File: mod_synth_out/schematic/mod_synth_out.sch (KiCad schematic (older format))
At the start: 3 parts

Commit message: Initial clone of befaco (without cue)
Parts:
- removed J?: Headphones, symbol Connector:AudioJack3
- added C? (x4): 10uf, Capacitor_THT:CP_Radial_D5.0mm_P2.00mm, symbol Device:CP_Small
- added C? (x4): 10pf, Capacitor_THT:C_Disc_D9.0mm_W2.5mm_P5.00mm, symbol Device:C_Small
- added C? (x8): 100nf, Capacitor_THT:C_Disc_D9.0mm_W2.5mm_P5.00mm, symbol Device:C_Small
- added D? (x2): LED, symbol Device:LED
- added D? (x4): 1N4148, Diode_THT:D_DO-35_SOD27_P7.62mm_Horizontal, symbol Diode:1N4148
- added J?: L OUT, symbol Connector:AudioJack3_SwitchTR
- added J?: R OUT, symbol Connector:AudioJack3_SwitchTR
- added J?: Phones, symbol Connector:AudioJack3_SwitchTR
- added J?: Conn_02x08_Odd_Even, symbol Connector_Generic:Conn_02x08_Odd_Even
- added Q? (x2): 2N3904, Package_TO_SOT_THT:TO-92_Inline, symbol Transistor_BJT:2N3904
- added R? (x4): 100k, Resistor_THT:R_Axial_DIN0207_L6.3mm_D2.5mm_P10.16mm_Horizontal, symbol Device:R
- added R? (x2): 39k, Resistor_THT:R_Axial_DIN0207_L6.3mm_D2.5mm_P10.16mm_Horizontal, symbol Device:R
- added R? (x6): 1k, Resistor_THT:R_Axial_DIN0207_L6.3mm_D2.5mm_P10.16mm_Horizontal, symbol Device:R
- added R? (x8): 10k, Resistor_THT:R_Axial_DIN0207_L6.3mm_D2.5mm_P10.16mm_Horizontal, symbol Device:R
- added R? (x4): 75, Resistor_THT:R_Axial_DIN0207_L6.3mm_D2.5mm_P10.16mm_Horizontal, symbol Device:R
- added RV? (x4): 100k, symbol Device:R_POT_Dual_Separate
- added U? (x6): TL072, symbol Amplifier_Operational:TL072
- added U? (x6): NE5532, symbol Amplifier_Operational:NE5532
- J?: value R IN -> L IN; footprint (none) -> Connector_Audio:Jack_3.5mm_QingPu_WQP-PJ398SM_Vertical_CircularHoles
- J?: value L IN -> R IN; footprint (none) -> Connector_Audio:Jack_3.5mm_QingPu_WQP-PJ398SM_Vertical_CircularHoles
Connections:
- net GND: now reaches J?.S
- net GND: now also J?.S, C?.2, C?.2, J?.S, Q?.1 (E), Q?.1 (E), R?.2, R?.2, R?.2, R?.2, RV?.1, RV?.1, RV?.4, RV?.4, U?.3 (+), U?.3 (+), U?.5 (+), U?.5 (+), U?.5 (+), U?.5 (+)
- net IN_L: now reaches J?.T
- net IN_L: now also J?.TN, R?.2, R?.2
- net IN_R: now reaches J?.T
- net IN_R: now also R?.2, R?.2
- new net: J?.R, R?.1 (x2)
- new net: J?.T, R?.1 (x2)
- new net: J?.R, R?.1, R?.1
- new net: J?.T, R?.1, R?.1
- new net: C?.1, C?.1, R?.1, U?.1
- new net: C?.2, R?.1, R?.2, U?.2 (-)
- new net: C?.2, R?.1, R?.2, U?.6 (-)
- new net: C?.1, C?.1, R?.1, U?.7
- new net: C?.1, D?.1 (K), D?.2 (A), R?.1, R?.2, U?.1
- new net: R?.1, U?.2 (-)
- new net: R?.1, U?.6 (-)
- new net: C?.1, D?.1 (K), D?.2 (A), R?.1, R?.2, U?.7
- new net: R?.2, U?.1, U?.2 (-) (x2)
- new net: R?.1, R?.2, U?.3 (+), U?.7 (x2)
- new net: R?.1, R?.2, U?.6 (-) (x2)
- new net: C?.2, RV?.3, RV?.3
- new net: C?.2, RV?.6, RV?.6
- new net: D?.1 (K), R?.2 (x2)
- new net: Q?.3 (C), R?.1 (x2)
- new net: Q?.2 (B), R?.1 (x2)
- new net +12V: D?.1 (K), D?.1 (K), D?.2 (A), D?.2 (A)
- new net -12V: D?.2 (A), D?.2 (A)
- new net A_POT_ML: RV?.2
- new net A_POT_MR: RV?.5
- new net A_POT_PH_L: RV?.2
- new net A_POT_PH_R: RV?.5
- new net B_POT_ML: R?.2
- new net B_POT_MR: R?.2
- new net B_POT_PH_L: R?.2
- new net B_POT_PH_R: R?.2
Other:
- moved on the sheet: J?

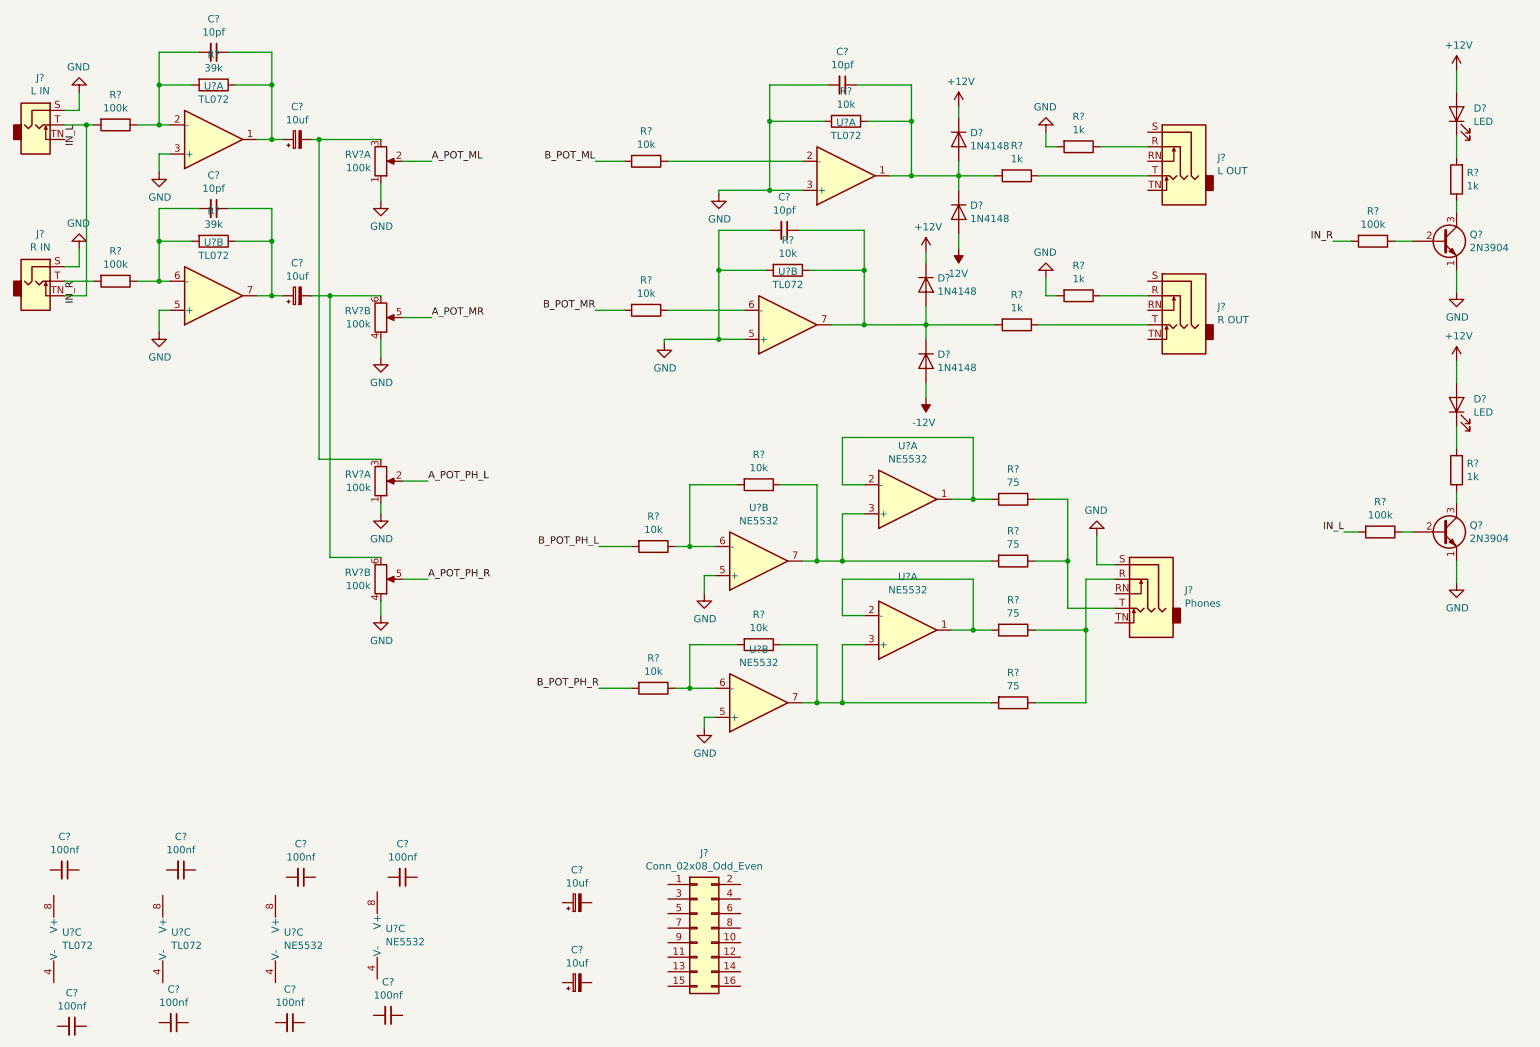
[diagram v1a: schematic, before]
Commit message: Attempt layout of output with through hole devices
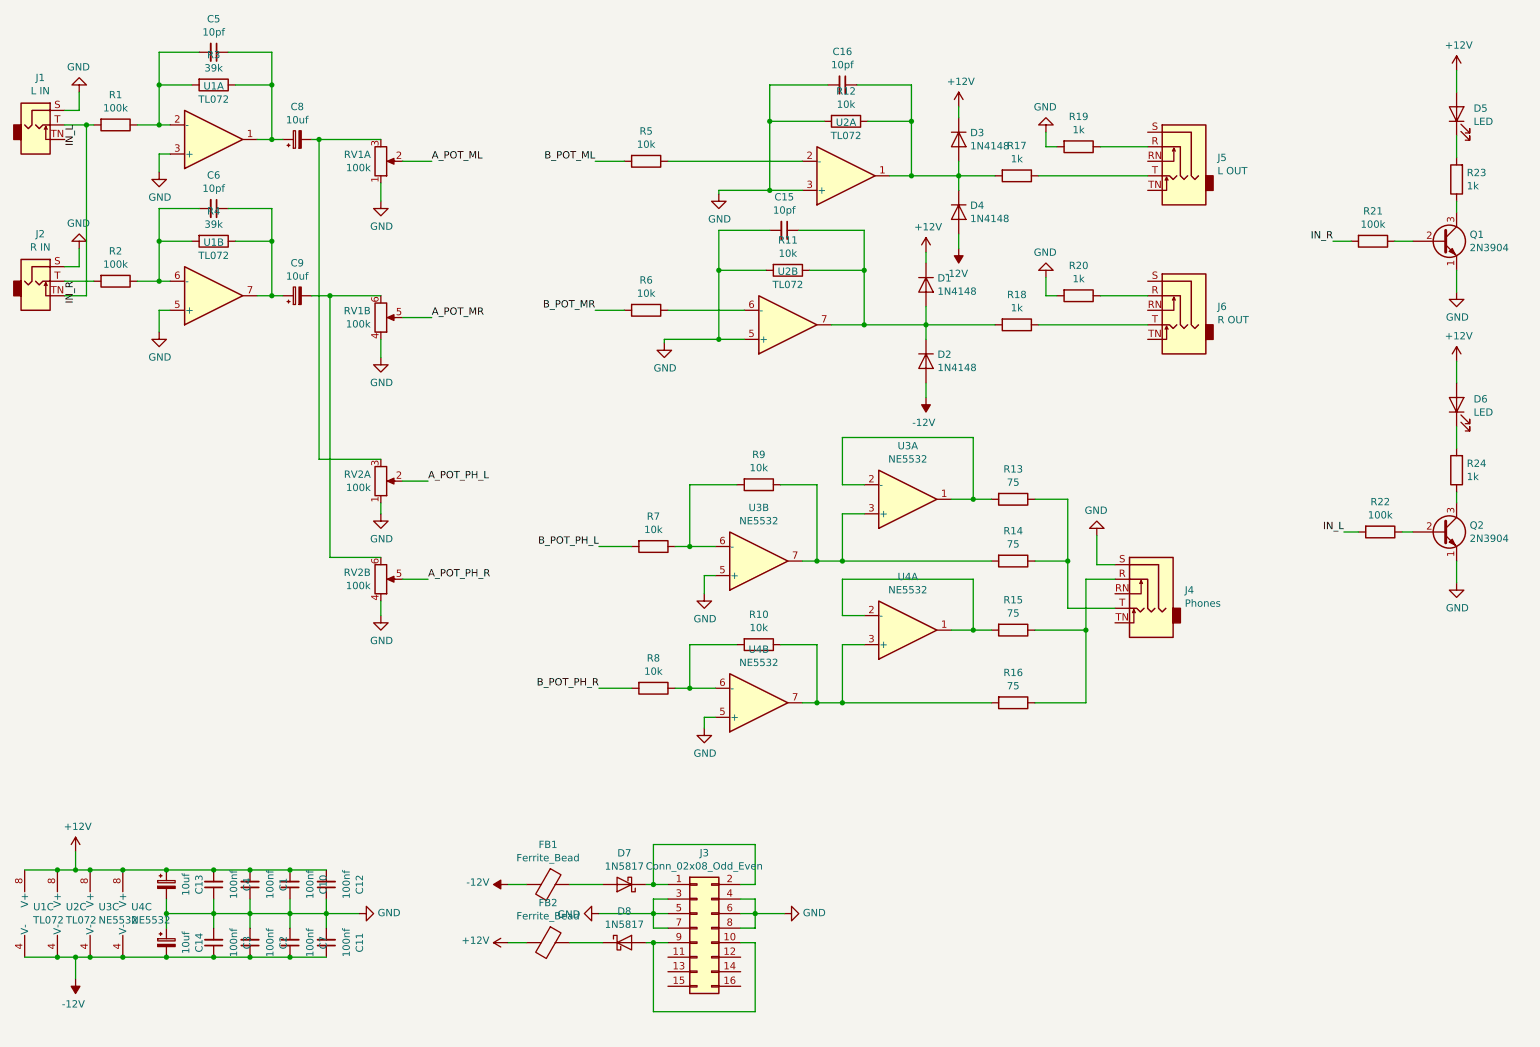
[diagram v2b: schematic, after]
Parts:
- added D7, D8: 1N5817, Diode_THT:D_DO-41_SOD81_P10.16mm_Horizontal, symbol Diode:1N5817
- added FB1, FB2: Ferrite_Bead, Resistor_THT:R_Axial_DIN0207_L6.3mm_D2.5mm_P10.16mm_Horizontal, symbol Device:Ferrite_Bead
- D5, D6: renamed from D?; footprint (none) -> LED_THT:LED_D5.0mm
- J3: renamed from J?; footprint (none) -> Connector_IDC:IDC-Header_2x08_P2.54mm_Vertical
- J4, J5, J6: renamed from J?; footprint (none) -> mod_synth:WQP-PJ612A-A
- RV1: renamed from RV?; footprint (none) -> Potentiometer_THT:Potentiometer_Alpha_RD902F-40-00D_Dual_Vertical_CircularHoles; Text (none) -> Volume
- RV1, RV2: renamed from RV?; footprint (none) -> Potentiometer_THT:Potentiometer_Alpha_RD902F-40-00D_Dual_Vertical_CircularHoles
- RV2: renamed from RV?; footprint (none) -> Potentiometer_THT:Potentiometer_Alpha_RD902F-40-00D_Dual_Vertical_CircularHoles; Text (none) -> Phones
- U1, U2, U3, U4: renamed from U?; footprint (none) -> Package_DIP:DIP-8_W7.62mm_Socket_LongPads
- gave numbers to parts that had none: 52
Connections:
- net +12V: now also C1.2, C10.2, C12.2, C13.1, C4.2, U1.8 (V+), U2.8 (V+), U3.8 (V+), U4.8 (V+), FB2.2
- net -12V: now also C11.1, C14.2, C2.1, C3.1, C7.1, U1.4 (V-), U2.4 (V-), U3.4 (V-), U4.4 (V-), FB1.2
- net GND: now also C1.1, C10.1, C11.2, C12.1, C13.2, C14.1, C2.2, C3.2, C4.1, C7.2, J3.3 (Pin_3), J3.4 (Pin_4), J3.5 (Pin_5), J3.6 (Pin_6), J3.7 (Pin_7), J3.8 (Pin_8)
- net at J3.1 (Pin_1): now also J3.2 (Pin_2), D7.1 (K)
- net at J3.10 (Pin_10): now also J3.9 (Pin_9), D8.2 (A)
- new net: D8.1 (K), FB2.1
- new net: D7.2 (A), FB1.1
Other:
- moved on the sheet: C1, C10, C11, C12, C13, C14, C2, C3, C4, C7, U1C, U2C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

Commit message: Attmept layout of output pcb on large pcb
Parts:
- added J7: Conn_01x07_Female, Connector_PinSocket_2.54mm:PinSocket_1x07_P2.54mm_Vertical, symbol Connector:Conn_01x07_Female
- added J8: Conn_01x07_Male, Connector_PinHeader_2.54mm:PinHeader_1x07_P2.54mm_Vertical, symbol Connector:Conn_01x07_Male
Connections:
- net +12V: now also J7.7 (Pin_7); no longer C10.2, D5.2 (A), D6.2 (A), U1.8 (V+)
- net -12V: now also J7.6 (Pin_6); no longer C7.1, U1.4 (V-)
- net A_POT_ML: now also J8.2 (Pin_2)
- net A_POT_MR: now also J8.3 (Pin_3)
- net A_POT_PH_L: now also J8.4 (Pin_4)
- net A_POT_PH_R: now also J8.5 (Pin_5)
- net B_POT_ML: now also J7.2 (Pin_2)
- net B_POT_MR: now also J7.3 (Pin_3)
- net B_POT_PH_L: now also J7.4 (Pin_4)
- net B_POT_PH_R: now also J7.5 (Pin_5)
- net GND: now also J7.1 (Pin_1); no longer C10.1, C7.2, J1.S, J2.S, Q1.1 (E), Q2.1 (E), RV1.1, RV1.4, RV2.1, RV2.4, U1.3 (+), U1.5 (+)
- new net +12_PCB_B: C10.2, D5.2 (A), D6.2 (A), J8.7 (Pin_7), U1.8 (V+)
- new net -12_PCB_B: C7.1, J8.6 (Pin_6), U1.4 (V-)
- new net GND_PCB_B: C10.1, C7.2, J1.S, J2.S, J8.1 (Pin_1), Q1.1 (E), Q2.1 (E), RV1.1, RV1.4, RV2.1, RV2.4, U1.3 (+), U1.5 (+)
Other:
- moved on the sheet: C10, C7, U1C

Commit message: Finish huge output pcb
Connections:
- net GND: now also J5.S, J6.S
- no-connect marks 0 -> 4
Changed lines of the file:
@@
 	2450 6475 2450 6425
 Connection ~ 2825 6475
+NoConn ~ 8250 4875
+NoConn ~ 8250 4675
+NoConn ~ 8475 1700
+NoConn ~ 8475 1900
+$Comp
+L power:GND #PWR?
+U 1 1 5D75DB78
+P 8400 1375
+F 0 "#PWR?" H 8400 1125 50  0001 C CNN
+F 1 "GND" H 8405 1202 50  0000 C CNN
+F 2 "" H 8400 1375 50  0001 C CNN
+F 3 "" H 8400 1375 50  0001 C CNN
+	1    8400 1375
+	-1   0    0    1
+$EndComp
+Wire Wire Line
+	8400 1375 8400 1500
+Wire Wire Line
+	8400 1500 8475 1500
+$Comp
+L power:GND #PWR?
+U 1 1 5D771850
+P 8400 2475
+F 0 "#PWR?" H 8400 2225 50  0001 C CNN
+F 1 "GND" H 8405 2302 50  0000 C CNN
+F 2 "" H 8400 2475 50  0001 C CNN
+F 3 "" H 8400 2475 50  0001 C CNN
+	1    8400 2475
+	-1   0    0    1
+$EndComp
+Wire Wire Line
+	8475 2525 8400 2525
+Wire Wire Line
+	8400 2525 8400 2475
 $EndSCHEMATC
